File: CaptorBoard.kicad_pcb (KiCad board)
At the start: 2 copper layers, 65 x 45 mm, 26 parts, among them J1 Conn_01x06, J2 MKDSN 1,5/ 4-5,08, SW1 SKHHLVA010, SW2 SKHHLVA010, U1 WeMos_mini, U2 IRM-02-5, U3 MOC3040X, U4 MOC3040X, U5 DHT22

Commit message: New routing
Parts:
- removed R15: 1k, Resistor_SMD:R_1210_3225Metric_Pad1.42x2.65mm_HandSolder
- removed U5: DHT22, pfo:DHT22_Temperature_Humidity
- added C1: 0.1µ, Capacitor_SMD:C_1210_3225Metric_Pad1.33x2.70mm_HandSolder, F.Cu at (104.4, 67.3)
- added C2: 12p, Capacitor_SMD:C_1210_3225Metric_Pad1.33x2.70mm_HandSolder, F.Cu at (120.2, 86.2)
- added C3: 12p, Capacitor_SMD:C_1210_3225Metric_Pad1.33x2.70mm_HandSolder, F.Cu at (120.2, 94.6)
- added C4: 22µ, Capacitor_SMD:C_1210_3225Metric_Pad1.33x2.70mm_HandSolder, F.Cu at (108.8, 71.8)
- added C5: 0.1µ, Capacitor_SMD:C_1210_3225Metric_Pad1.33x2.70mm_HandSolder, F.Cu at (108.8, 75.1)
- added C6: 1µ, Capacitor_SMD:C_1210_3225Metric_Pad1.33x2.70mm_HandSolder, F.Cu at (113.4, 72.7)
- added D1: REL1, LED_SMD:LED_1210_3225Metric_Pad1.42x2.65mm_HandSolder, F.Cu at (131.6, 93.1)
- added D11: MRA4007T3G, Diode_SMD:D_SMA, F.Cu at (144.0, 87.7)
- added D2: MRA4007T3G, Diode_SMD:D_SMA, F.Cu at (132.3, 87.9)
- added D8: REL2, LED_SMD:LED_1210_3225Metric_Pad1.42x2.65mm_HandSolder, F.Cu at (143.5, 93.5)
- added J3: Screw_Terminal_01x06, TerminalBlock_Phoenix:TerminalBlock_Phoenix_MKDS-1,5-6-5.08_1x06_P5.08mm_Horizontal, F.Cu at (145.2, 55.2)
- added J4: Conn_01x07, Connector_PinHeader_2.54mm:PinHeader_1x07_P2.54mm_Vertical, F.Cu at (129.4, 98.2)
- added J5: Conn_01x04, Connector_PinHeader_2.54mm:PinHeader_1x04_P2.54mm_Vertical, F.Cu at (118.1, 98.2)
- added K1: G5LE-1-DC5, Relay_THT:Relay_SPDT_Omron-G5LE-1, F.Cu at (124.0, 81.3)
- added K2: G5LE-1-DC5, Relay_THT:Relay_SPDT_Omron-G5LE-1, F.Cu at (141.1, 81.3)
- added PS1: IRM-05-5, Converter_ACDC:Converter_ACDC_MeanWell_IRM-05-xx_THT, F.Cu at (161.7, 95.9)
- added Q1: 2N7002E, Package_TO_SOT_SMD:SOT-23, F.Cu at (128.4, 87.3)
- added Q2: 2N7002E, Package_TO_SOT_SMD:SOT-23, F.Cu at (140.0, 87.3)
- added R1: 1k, Resistor_SMD:R_1210_3225Metric_Pad1.30x2.65mm_HandSolder, F.Cu at (104.4, 72.5)
- added R2: 5M, Resistor_SMD:R_1210_3225Metric_Pad1.30x2.65mm_HandSolder, F.Cu at (119.4, 90.5)
- added R3: 10k, Resistor_SMD:R_1210_3225Metric_Pad1.30x2.65mm_HandSolder, F.Cu at (108.8, 78.4)
- added R4: 1k, Resistor_SMD:R_1210_3225Metric_Pad1.30x2.65mm_HandSolder, F.Cu at (124.6, 86.8)
- added R5: 1k, Resistor_SMD:R_1210_3225Metric_Pad1.30x2.65mm_HandSolder, F.Cu at (126.9, 91.8)
- added R6: 1k, Resistor_SMD:R_1210_3225Metric_Pad1.30x2.65mm_HandSolder, F.Cu at (136.1, 86.9)
- added Y1: CM9V-T1A-32.768kHz-7pF-20PPM-TA-QC, Crystal:Crystal_SMD_MicroCrystal_CM9V-T1A-2Pin_1.6x1.0mm_HandSoldering, F.Cu at (121.9, 90.4)
- D3, D4, D5, D6, D7: footprint LED_THT:LED_D3.0mm -> LED_SMD:LED_1210_3225Metric_Pad1.42x2.65mm_HandSolder
- J2: value MKDSN 1,5/ 4-5,08 -> Screw_Terminal_01x03; footprint TerminalBlock_Phoenix:TerminalBlock_Phoenix_MKDS-1,5-4-5.08_1x04_P5.08mm_Horizontal -> TerminalBlock_Phoenix:TerminalBlock_Phoenix_MKDS-1,5-3-5.08_1x03_P5.08mm_Horizontal
- R10, R11, R12, R13, R14, R7, R8, R9: footprint Resistor_SMD:R_1210_3225Metric_Pad1.42x2.65mm_HandSolder -> Resistor_SMD:R_1210_3225Metric_Pad1.30x2.65mm_HandSolder
- U1: value WeMos_mini -> ESP32-WROOM-32E-N4; footprint wemos-d1-mini:wemos-d1-mini-with-pin-header-and-connector -> Espressif:ESP32-WROOM-32E
- U2: value IRM-02-5 -> TC1264-3.3VDBTR; footprint Converter_ACDC:Converter_ACDC_MeanWell_IRM-02-xx_THT -> Package_TO_SOT_SMD:SOT-223-3_TabPin2
- moved U3 74.5 mm to (177.6, 61.2)
- moved R12 74.3 mm to (167.0, 51.8)
- moved U4 74.1 mm to (177.6, 52.1)
- moved D10 64.2 mm to (187.3, 71.8), turned to 180 degrees
- moved J1 63.8 mm to (148.3, 86.0), turned to 0 degrees
- moved R13 63.5 mm to (156.5, 51.8)
- moved D9 58.1 mm to (179.7, 75.9), turned to 0 degrees
- moved F1 55.9 mm to (183.8, 80.6), turned to 0 degrees
- moved D3 53.9 mm to (113.5, 52.5), turned to 90 degrees
- moved J2 49.2 mm to (184.7, 97.0)
- moved D4 45.3 mm to (107.1, 52.5), turned to 90 degrees
- moved R7 42.8 mm to (113.5, 57.6), turned to -90 degrees
- moved R14 41.9 mm to (138.3, 92.4), turned to -90 degrees
- moved D6 37.5 mm to (103.6, 52.5), turned to 90 degrees
- moved R8 31.5 mm to (107.1, 57.6)
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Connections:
- J1 pad 6: +3V3 -> +3.3V
- J2 pad 1: (no net) -> /Neutre
- J2 pad 2: /CMD2 -> /Phase_in
- J2 pad 3: /Phase_in -> /CMD2
- R14 pad 1: +3V3 -> +5V
- R14 pad 2: /PILOT_1 -> Net-(D8-Pad2)
- U1 pad 1: +5V -> GND
- U1 pad 11: /PILOT_2 -> /PILOT_1
- U1 pad 12: /CONF-1°C -> /PILOT_2
- U1 pad 13: /ECO -> /CONF
- U1 pad 14: /CAPTOR -> /CONF-1°C
- U1 pad 15: /CONF-2°C -> GND
- U1 pad 16: +3V3 -> /CONF-2°C
- U1 pad 2: GND -> +3.3V
- U1 pad 3: /PILOT_1 -> /RESET
- U1 pad 4: /SELECT -> unconnected-(U1-Pad4)
- U1 pad 5: /SDA_EXT -> unconnected-(U1-Pad5)
- U1 pad 6: /SCL_EXT -> /GPIO34
- U1 pad 7: /CONF -> /GPIO35
- U1 pad 8: /POWER -> /XP
- U1 pad 9: /RESET -> /XN
- U2 pad 1: /Neutre -> +5V
- U2 pad 2: /Phase -> GND
- U2 pad 3: GND -> +3.3V
- U3 pad 3: (no net) -> unconnected-(U3-Pad3)
- U3 pad 5: (no net) -> unconnected-(U3-Pad5)
- U4 pad 3: (no net) -> unconnected-(U4-Pad3)
- U4 pad 5: (no net) -> unconnected-(U4-Pad5)
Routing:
- net +3.3V: track 0.00 -> 102.2 mm, vias 0 -> 2
- net /PILOT_2: track 13.2 -> 92.6 mm, vias 0 -> 2
- net GND: track 131.1 -> 56.6 mm, vias 0 -> 20
- net /PILOT_1: track 35.6 -> 99.8 mm
- net /GPIO35: track 0.00 -> 61.6 mm, vias 0 -> 1
- net /GPIO23: track 0.00 -> 59.0 mm, vias 0 -> 1
- net /GPIO34: track 0.00 -> 56.5 mm, vias 0 -> 1
- net /RX: track 0.00 -> 50.6 mm, vias 0 -> 1
- net /TX: track 0.00 -> 49.4 mm, vias 0 -> 1
- net /GPIO5: track 0.00 -> 46.2 mm, vias 0 -> 1
- net /GPIO17: track 0.00 -> 46.2 mm, vias 0 -> 1
- net +3V3: track 41.9 -> 0.00 mm
- net /REL2: track 0.00 -> 40.5 mm, vias 0 -> 2
- net /SCL_EXT: track 18.9 -> 57.4 mm, vias 0 -> 1
- net /SDA_EXT: track 22.5 -> 60.4 mm, vias 0 -> 1
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- added copper zone on B.Cu, net GND
- added copper zone on F.Cu, net GND
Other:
- board size 65 x 45 mm -> 95 x 50 mm
- board text added: "1 - 3.3V 2 - Captor 3 - 4 - GND"
- board text added: "1 - 5V 2 - SDC 3 - SDA 4 - GND 5 - Ana 6 - 3.3V"
- board text added: "1 - TX 2 - RX 3 - GPIO5 4 - GPIO17 5 - GPIO23 6 - GPIO34 7 - GPIO35"
- board text added: "CMD"
- board text added: "COM"
- board text added: "Conf -1°C"
- board text added: "Conf -2°C"
- board text added: "Eco"
- board text added: "L"
- board text added: "N"
- board text added: "NC"
- board text added: "NO"
- board text added: "Pwd"
- board text added: "REL 1"
- board text added: "REL 2"
- board text removed: "-1°C"
- board text removed: "-2°C"
- board text removed: "1 - +5V 2 - CAPTEUR 3 - NC 4 - GND"
- board text removed: "1 - +5V 2 - SCL 3 - SDA 4 - GND 5 - ANA 6 - +3.3V"
- board text removed: "1 - Terre 2 - Pilote 3 - Phase 4 - Neutre"
- board text removed: "ECO"
- board text removed: "Reset"
- board text removed: "Select"
- board text removed: "Status"

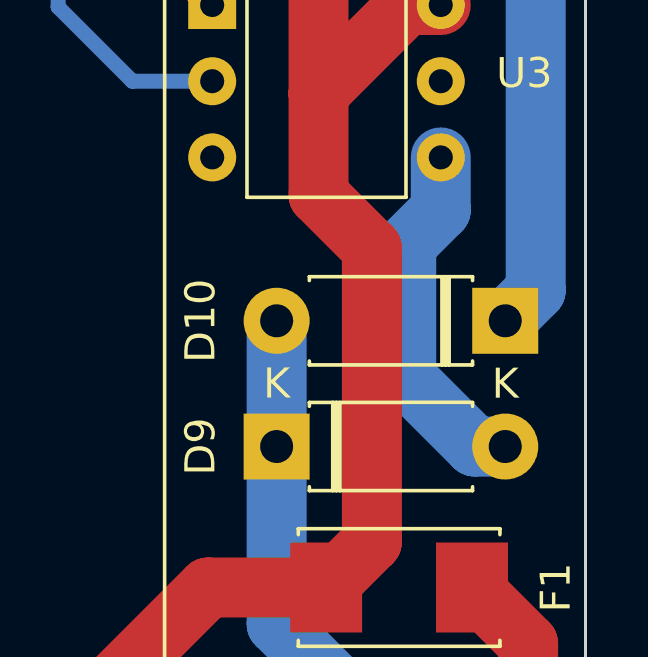
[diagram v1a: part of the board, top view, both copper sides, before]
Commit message: move sector track for more isolating
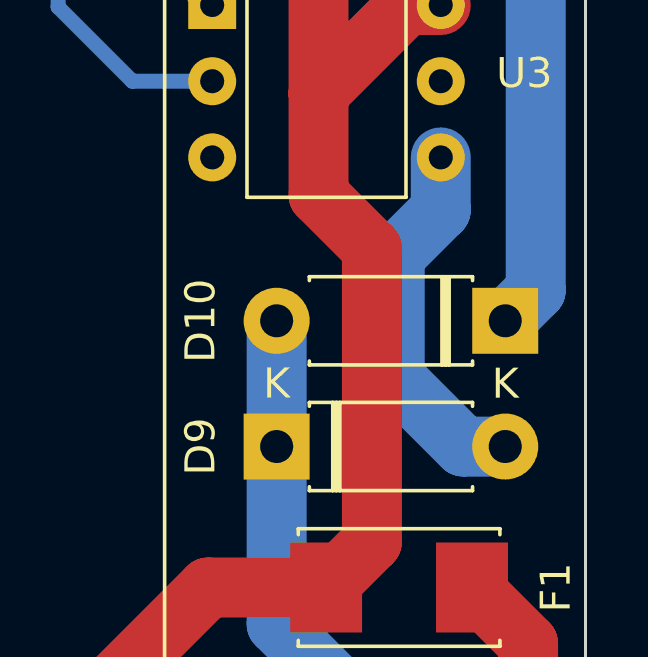
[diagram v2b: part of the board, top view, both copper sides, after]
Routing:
- net /P1: track 12.1 -> 12.6 mm
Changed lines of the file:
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@@
   (segment (start 188.087 82.516) (end 186.216 80.645) (width 2) (layer "F.Cu") (net 26))
   (segment (start 186.817 91.948) (end 188.087 90.678) (width 2) (layer "F.Cu") (net 26))
-  (segment (start 185.176 68.062) (end 184.023 69.215) (width 2) (layer "B.Cu") (net 27))
-  (segment (start 184.023 69.215) (end 184.023 73.66) (width 2) (layer "B.Cu") (net 27))
-  (segment (start 184.023 73.66) (end 186.309 75.946) (width 2) (layer "B.Cu") (net 27))
-  (segment (start 186.309 75.946) (end 187.325 75.946) (width 2) (layer "B.Cu") (net 27))
+  (segment (start 183.642 73.66) (end 185.928 75.946) (width 2) (layer "B.Cu") (net 27))
+  (segment (start 185.176 68.062) (end 183.642 69.596) (width 2) (layer "B.Cu") (net 27))
+  (segment (start 183.642 69.596) (end 183.642 73.66) (width 2) (layer "B.Cu") (net 27))
+  (segment (start 185.928 75.946) (end 187.325 75.946) (width 2) (layer "B.Cu") (net 27))
   (segment (start 185.176 66.309) (end 185.176 68.062) (width 2) (layer "B.Cu") (net 27))
   (segment (start 186.07 57.165) (end 185.176 57.165) (width 2) (layer "B.Cu") (net 28))

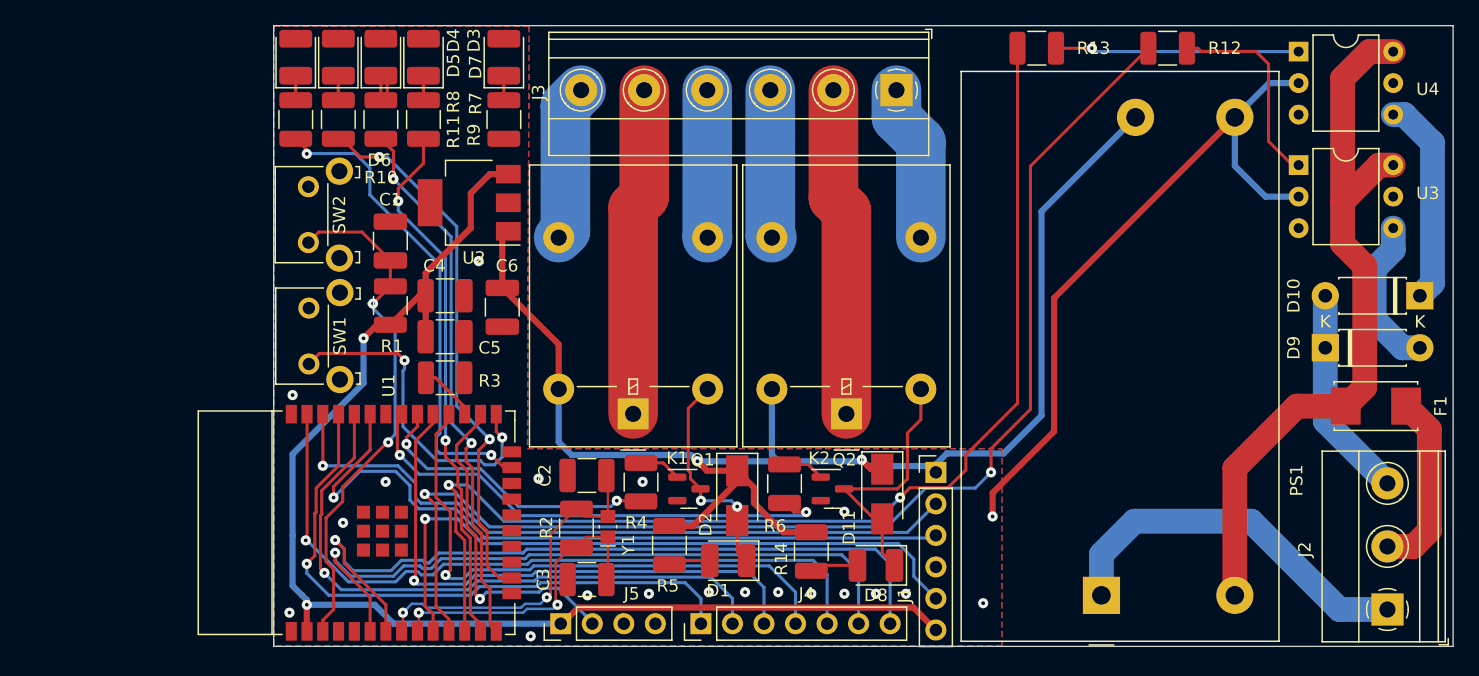
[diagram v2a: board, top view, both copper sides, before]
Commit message: Change routing and add logo
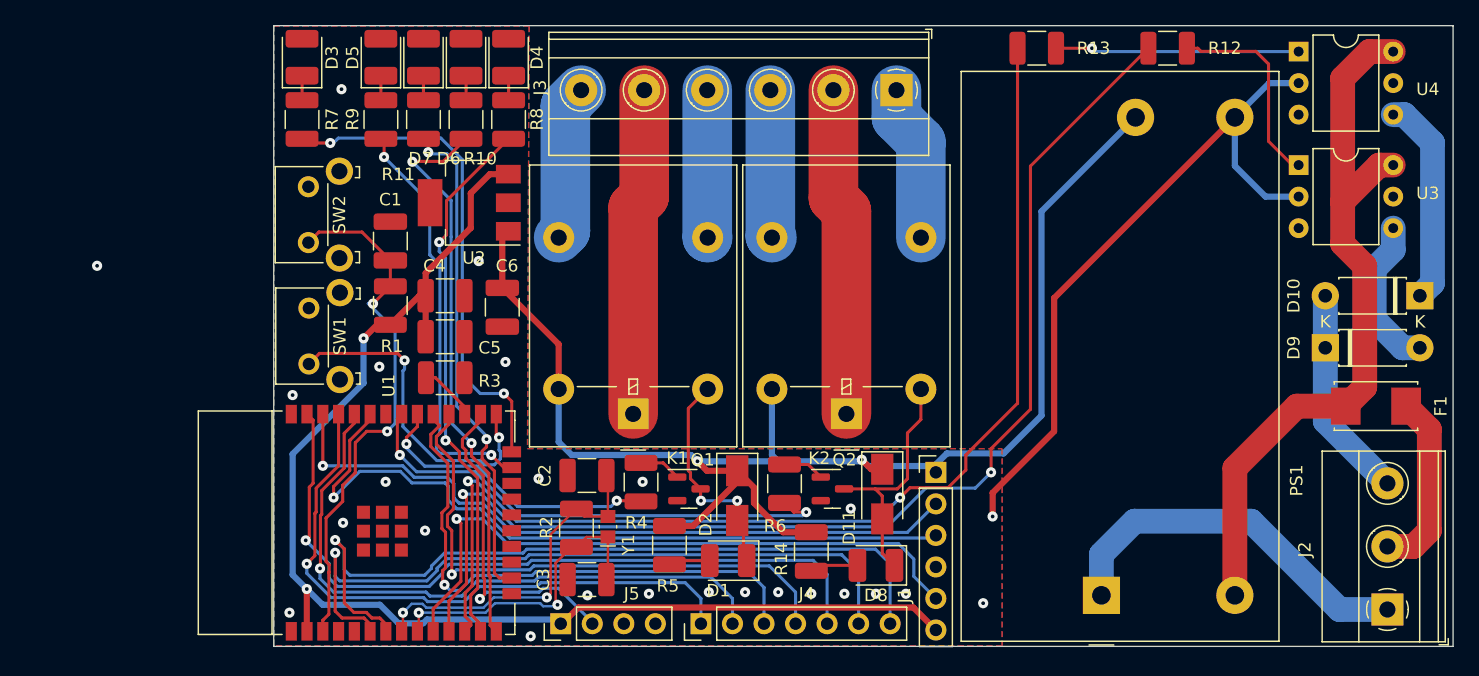
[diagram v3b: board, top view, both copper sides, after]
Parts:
- added REF**: OSHW-Logo2_9.8x8mm_SilkScreen, Symbol:OSHW-Logo2_9.8x8mm_SilkScreen, B.Cu at (104.4, 91.8)
- moved D3 16.3 mm to (97.3, 52.5)
- moved R7 16.3 mm to (97.3, 57.6)
- moved D5 6.86 mm to (103.6, 52.5)
- moved D7 6.86 mm to (107.1, 52.5)
- moved R11 6.86 mm to (107.1, 57.6)
- moved R9 6.86 mm to (103.6, 57.6)
- moved D4 6.86 mm to (113.9, 52.5)
- moved D6 6.86 mm to (110.5, 52.5)
- moved R10 6.86 mm to (110.5, 57.6)
- moved R8 6.86 mm to (113.9, 57.6)
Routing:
- net /POWER: track 0.00 -> 40.2 mm, vias 0 -> 2
- net /ECO: track 39.0 -> 33.8 mm
- net /CONF-2°C: track 43.9 -> 40.0 mm
- net /PILOT_1: track 99.8 -> 96.6 mm
- net /GPIO34: track 56.5 -> 58.5 mm
- net /CONF-1°C: track 43.9 -> 45.7 mm
- net /ANA: track 54.0 -> 52.2 mm
- net Net-(D6-Pad1): track 3.57 -> 1.98 mm
- net /GPIO35: track 61.6 -> 63.2 mm
- net Net-(D11-Pad2): track 21.3 -> 19.9 mm
- net /GPIO23: track 59.0 -> 60.3 mm
- net /RX: track 50.6 -> 51.6 mm
- net /GPIO5: track 46.2 -> 45.3 mm
- net /PILOT_2: track 92.6 -> 91.7 mm
- net +3.3V: track 102.2 -> 103.0 mm
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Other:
- board text added: "Philippe12"

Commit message: update ref
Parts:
- removed REF**: OSHW-Logo2_9.8x8mm_SilkScreen, Symbol:OSHW-Logo2_9.8x8mm_SilkScreen
- added J6: Screw_Terminal_01x03, TerminalBlock_Phoenix:TerminalBlock_Phoenix_MKDS-1,5-3-5.08_1x03_P5.08mm_Horizontal, F.Cu at (129.0, 55.2)
- D1: value REL1 -> LTST-C930KGKT
- D3: value POWER -> LTST-C930KGKT
- D4: value CONF -> LTST-C930KGKT
- D5: value ECO -> LTST-C930KGKT
- D6: value CONF-1°C -> LTST-C930KGKT
- D7: value CONF-2°C -> LTST-C930KGKT
- D8: value REL2 -> LTST-C930KGKT
- J3: value Screw_Terminal_01x06 -> Screw_Terminal_01x03; footprint TerminalBlock_Phoenix:TerminalBlock_Phoenix_MKDS-1,5-6-5.08_1x06_P5.08mm_Horizontal -> TerminalBlock_Phoenix:TerminalBlock_Phoenix_MKDS-1,5-3-5.08_1x03_P5.08mm_Horizontal
- Y1: value CM9V-T1A-32.768kHz-7pF-20PPM-TA-QC -> CC7V-T1A-32.768kHz-12.5pF-100PPM-TA-QC; footprint Crystal:Crystal_SMD_MicroCrystal_CM9V-T1A-2Pin_1.6x1.0mm_HandSoldering -> Crystal:Crystal_SMD_MicroCrystal_CC7V-T1A-2Pin_3.2x1.5mm_HandSoldering
- moved R2 1.30 mm to (118.1, 90.2)
- moved J3 1.02 mm to (146.2, 55.2)
- moved Y1 0.91 mm to (121.0, 90.2)
- moved C2 0.57 mm to (120.0, 85.7), turned to 180 degrees
- moved C3 0.18 mm to (120.1, 94.7), turned to 180 degrees
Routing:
- net /XN: track 25.2 -> 22.1 mm
- net /CAPTOR: track 27.1 -> 26.3 mm
- net /XP: track 28.2 -> 28.8 mm
- net /GPIO5: track 45.3 -> 44.8 mm

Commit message: add serigraphie
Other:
- board text added: "Reset"
- board text added: "Select"
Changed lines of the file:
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@@
     (effects (font (size 1.7 1.7) (thickness 0.15)) (justify left mirror))
+  )
+  (gr_text "Reset" (at 95.377 65.151 180) (layer "B.SilkS")
+    (effects (font (size 2 2) (thickness 0.15)) (justify left mirror))
   )
   (gr_text "NC" (at 136.017 51.816 180) (layer "B.SilkS")
@@
     (effects (font (size 2 2) (thickness 0.15)) (justify left mirror))
   )
+  (gr_text "Select" (at 95.377 74.93 180) (layer "B.SilkS")
+    (effects (font (size 2 2) (thickness 0.15)) (justify left mirror))
+  )

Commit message: New desing
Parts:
- moved D3 45.5 mm to (106.9, 97.0)
- moved U2 41.7 mm to (141.9, 92.1), turned to 0 degrees
- moved R7 40.0 mm to (103.6, 97.1), turned to 90 degrees
- moved C1 30.3 mm to (110.5, 97.1)
- moved SW2 29.2 mm to (97.7, 96.7)
- moved R1 26.3 mm to (113.8, 97.1), turned to 90 degrees
- moved C4 26.0 mm to (125.1, 92.0), turned to 90 degrees
- moved C6 24.6 mm to (128.7, 92.0)
- moved SW1 19.4 mm to (97.7, 57.8)
- moved R3 19.3 mm to (98.0, 62.4), turned to 180 degrees
- moved C2 18.9 mm to (101.1, 86.6), turned to -90 degrees
- moved C5 16.3 mm to (97.5, 86.9), turned to -90 degrees
- moved U1 16.0 mm to (103.3, 74.0)
- moved Y1 15.3 mm to (105.8, 88.7), turned to 180 degrees
- moved R2 13.0 mm to (105.9, 85.8), turned to 0 degrees
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- renumbered J6 to locked
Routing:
- net /CAPTOR: track 26.3 -> 64.1 mm
- net /GPIO5: track 44.8 -> 74.2 mm
- net /GPIO17: track 45.7 -> 75.0 mm
- net +3.3V: track 103.0 -> 75.0 mm, vias 2 -> 0
- net /CONF-1°C: track 45.9 -> 24.6 mm
- net /XP: track 28.8 -> 10.3 mm, vias 2 -> 0
- net /CONF: track 43.6 -> 25.1 mm
- net /ECO: track 33.8 -> 17.0 mm
- net /CONF-2°C: track 39.9 -> 24.0 mm
- net /SCL_EXT: track 57.4 -> 70.9 mm
- net /POWER: track 40.2 -> 52.0 mm
- net /XN: track 22.1 -> 10.5 mm, vias 2 -> 0
- net /REL1: track 24.4 -> 35.4 mm
- net /RESET: track 43.2 -> 32.3 mm, vias 2 -> 1
- net Net-(Q1-Pad1): track 3.39 -> 14.3 mm, vias 0 -> 2
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
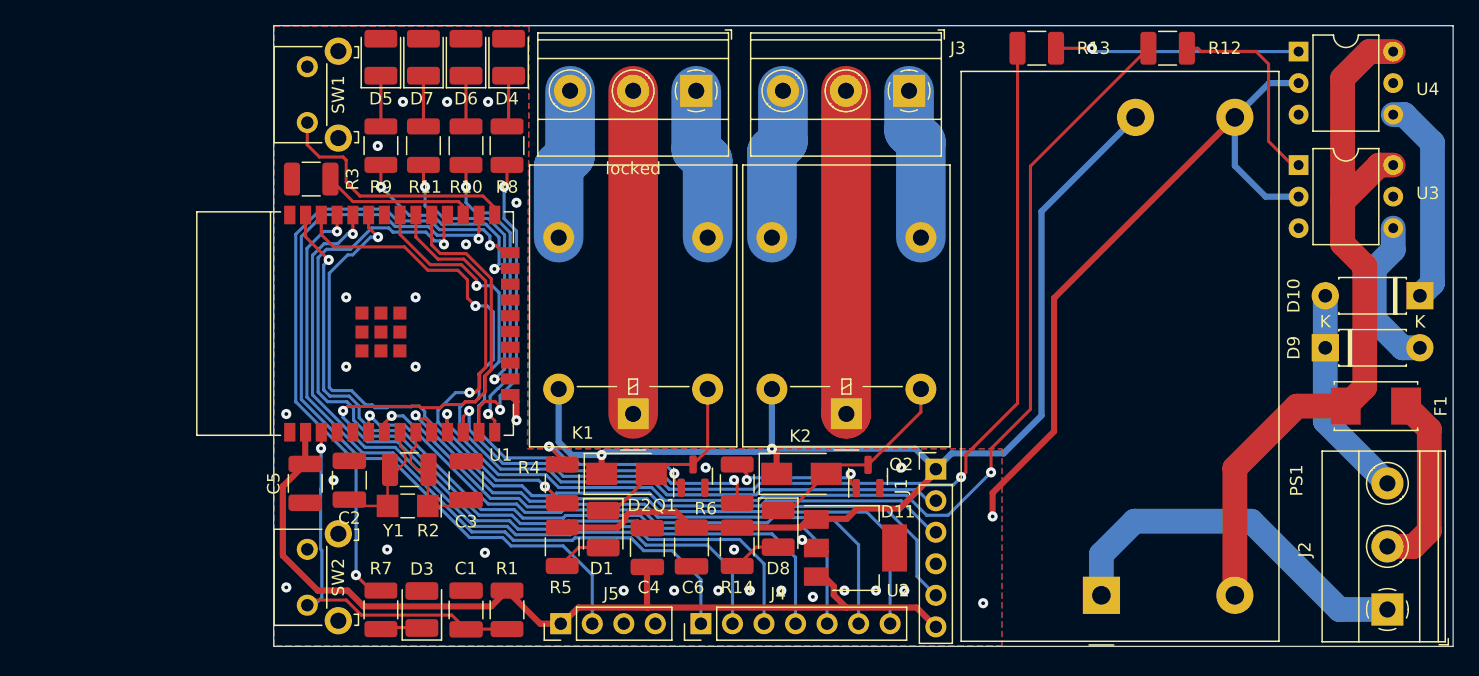
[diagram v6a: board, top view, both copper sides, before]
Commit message: Optimize routing
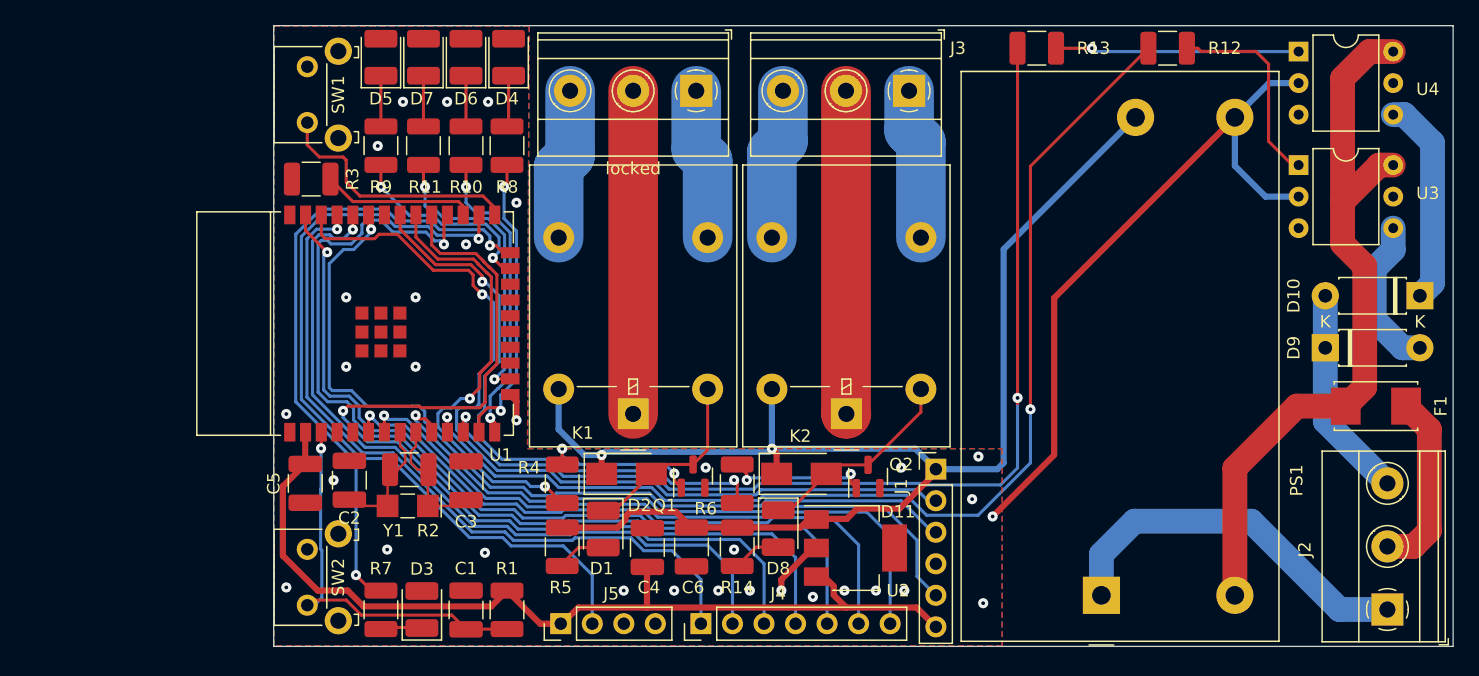
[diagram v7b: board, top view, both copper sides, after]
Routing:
- net GND: track 59.1 -> 63.9 mm, vias 31 -> 32
- net /PILOT_2: track 82.1 -> 84.3 mm
- net /GPIO17: track 75.0 -> 76.8 mm
- net Net-(Q1-Pad1): track 14.3 -> 12.8 mm
- net /GPIO5: track 74.2 -> 75.5 mm
- net /PILOT_1: track 90.3 -> 91.4 mm
- net /SCL_EXT: track 70.9 -> 72.1 mm
- net /REL1: track 35.4 -> 36.4 mm
- net /CONF: track 25.1 -> 24.3 mm
- net /RX: track 60.9 -> 61.6 mm

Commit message: Add open source hardware logo
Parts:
- added LOGO1: Logo_Open_Hardware_Large, Symbol:OSHW-Logo_11.4x12mm_SilkScreen, B.Cu at (105.5, 78.5)
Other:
- board text added: "Activity"
- board text removed: "Pwd"
